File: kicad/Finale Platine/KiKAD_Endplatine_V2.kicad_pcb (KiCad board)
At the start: 2 copper layers, 102 x 50 mm, 57 parts, among them J1 Conn_02x08_Odd_Even, J4 Conn_01x03_Pin, Q1 Q_NPN_ECB, Q2 Q_NPN_ECB, Q3 Q_NPN_ECB, Q4 Q_NPN_ECB, U1 NE555P, U2 TL074

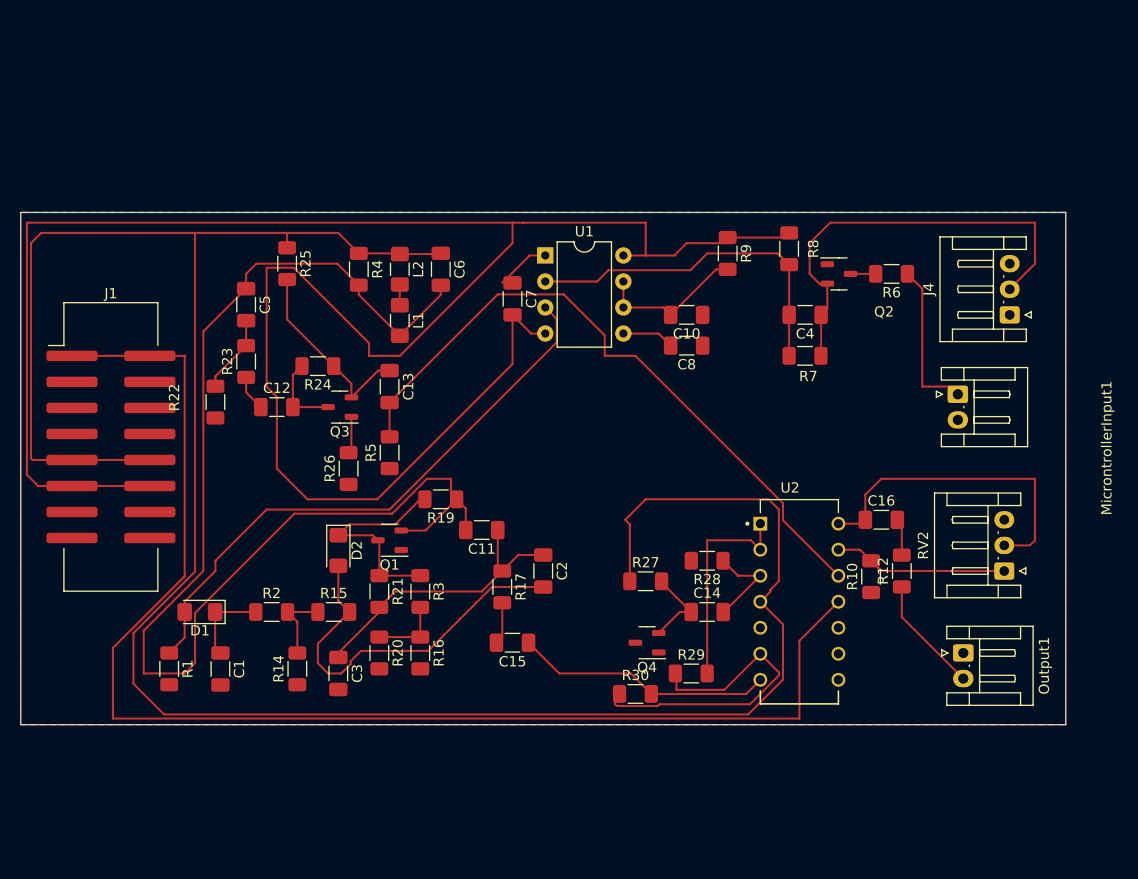
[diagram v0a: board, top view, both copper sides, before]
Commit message: Platinendesign update mit 2 Induktoren
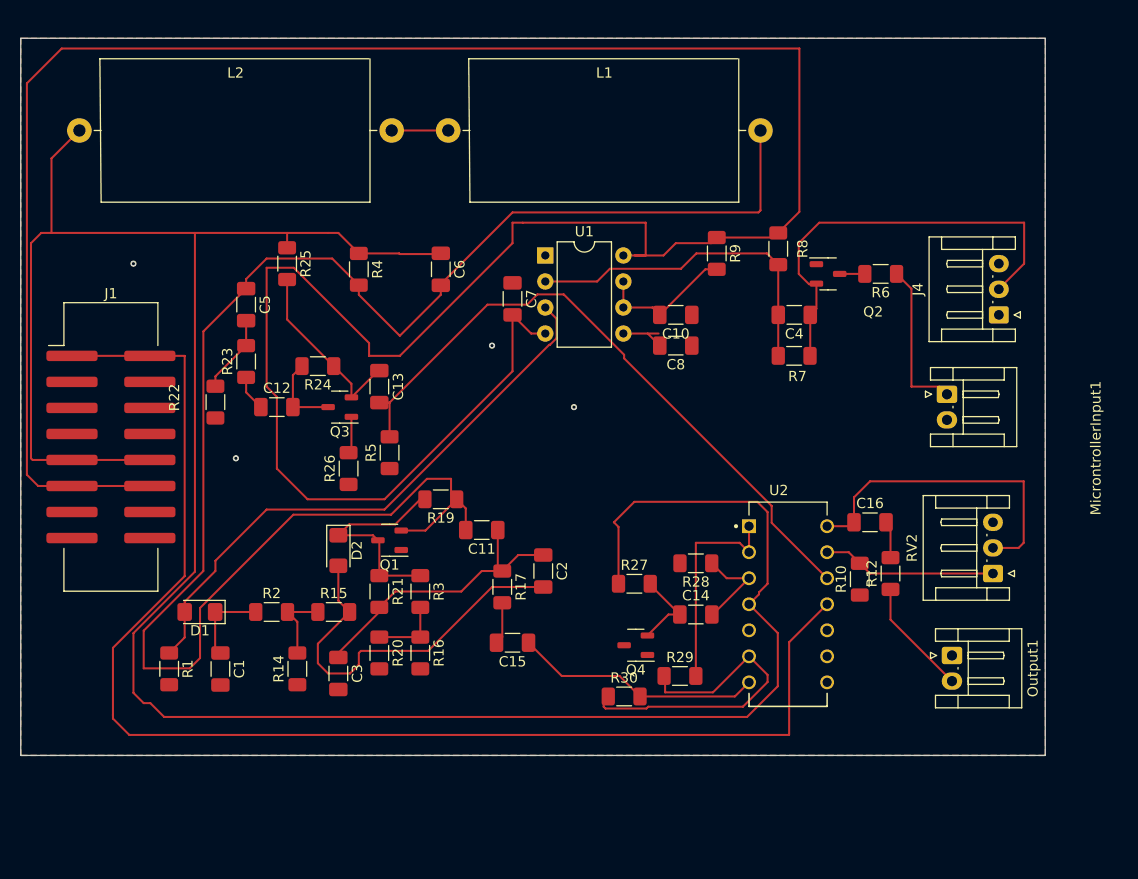
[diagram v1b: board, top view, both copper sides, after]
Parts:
- L1, L2: footprint Inductor_SMD:L_1206_3216Metric_Pad1.42x1.75mm_HandSolder -> TL074:L_Axial_L26.0mm_D14.0mm_P30.48mm_Horizontal_Fastron_JORIS
- moved L2 34.1 mm to (105.7, 44.0), turned to 0 degrees
- moved L1 19.1 mm to (141.7, 44.0), turned to 0 degrees
- moved C14 1.13 mm to (165.9, 91.2)
- moved C16 1.13 mm to (182.9, 82.2)
- moved Output1 1.13 mm to (190.9, 95.2)
- moved Q4 1.13 mm to (160.0, 94.2)
- moved R10 1.13 mm to (181.9, 87.8)
- moved R12 1.13 mm to (184.9, 87.2)
- moved R27 1.13 mm to (159.9, 88.2)
- moved R28 1.13 mm to (165.9, 86.2)
- moved R29 1.13 mm to (164.3, 97.2)
- moved R30 1.13 mm to (158.9, 99.2)
- moved RV2 1.13 mm to (194.9, 87.2)
- moved U2 1.13 mm to (174.9, 90.2)
- moved C10 1.06 mm to (163.9, 62.0)
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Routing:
- net +5V: track 211.4 -> 273.6 mm
- net Net-(Q1-C): track 121.6 -> 163.1 mm
- net +12V: track 228.6 -> 240.4 mm
- net GND: track 5.31 -> 0.00 mm, vias 0 -> 4
- net Net-(L1-Pad1): track 2.02 -> 5.52 mm
- net -12V: track 129.3 -> 130.4 mm
- net Net-(Q3-C): track 18.9 -> 17.8 mm
- net Net-(U1-TR): track 34.3 -> 33.2 mm
- net Net-(C15-Pad1): track 25.3 -> 24.3 mm
- net Net-(C13-Pad2): track 65.0 -> 64.1 mm
- net Net-(D2-A): track 37.3 -> 37.8 mm
- added copper zone on B.Cu, net GND
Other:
- board size 102 x 50 mm -> 100 x 70 mm

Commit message: Platinenupdate
Platine geupdatet Beschriftung mehr oder weniger gut
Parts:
- added +/L3: 100m, Inductor_THT:L_Radial_D12.0mm_P6.00mm_Murata_1900R, F.Cu at (113.0, 43.0)
- added C6/R1: 1000k, Resistor_SMD:R_1206_3216Metric_Pad1.30x1.75mm_HandSolder, F.Cu at (147.0, 110.0)
- added R12/-1: 100, Resistor_SMD:R_1206_3216Metric_Pad1.30x1.75mm_HandSolder, F.Cu at (142.0, 91.0)
- added RV1/-1: 10k, Connector_JST:JST_EH_S3B-EH_1x03_P2.50mm_Horizontal, F.Cu at (147.5, 87.5)
- +/L1: renamed from L1; value 560m -> 100m; footprint TL074:L_Axial_L26.0mm_D14.0mm_P30.48mm_Horizontal_Fastron_JORIS -> Inductor_THT:L_Radial_D12.0mm_P6.00mm_Murata_1900R
- +/L2: renamed from L2; value 560m -> 100m; footprint TL074:L_Axial_L26.0mm_D14.0mm_P30.48mm_Horizontal_Fastron_JORIS -> Inductor_THT:L_Radial_D12.0mm_P6.00mm_Murata_1900R
- D2: value D -> C5/D2
- moved +/L2 20.3 mm to (126.0, 43.0)
- moved C7/+1 13.4 mm to (157.0, 77.0)
- moved R1/R1 13.0 mm to (108.0, 107.8)
- moved R5/D1 12.5 mm to (110.0, 101.0)
- moved D1/R2 11.9 mm to (118.0, 101.0)
- moved +/C15 11.4 mm to (151.0, 105.0)
- moved -/-1 11.4 mm to (142.0, 106.0)
- moved C3/C1 11.3 mm to (119.3, 107.8)
- moved C6/R3 11.2 mm to (137.0, 106.0)
- moved C4/C2 10.4 mm to (147.0, 96.6)
- moved +/R17 10.0 mm to (153.0, 96.5)
- moved R7/-1 10.0 mm to (130.6, 101.0)
- moved R10/-1 9.49 mm to (142.0, 98.0)
- moved R9/+1 9.22 mm to (130.5, 106.2)
- moved +/+1 9.06 mm to (136.0, 98.0)
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- renumbered R21 to +/+1, C14 to +/C14, C15 to +/C15, C6 to +/C6, Q4 to +/Q4, R17 to +/R17, R27 to +/R27, R28 to +/R28, R29 to +/R29, R30 to +/R30, R16 to -/-1, C12 to C1/+1, C1 to C3/C1, C2 to C4/C2, R20 to C6/R3, C11 to C7/+1, C5 to C8/C5, C13 to C9/+1, R2 to D1/R2, Q3 to Q3/+1, R1 to R1/R1, R3 to R10/-1, R19 to R11/+1, R4 to R14/R4, R23 to R16/+1, R26 to R17/+1, R22 to R2/R5, R25 to R3/+1, R24 to R4/+1, D1 to R5/D1, R5 to R6/+1, R15 to R7/-1, R14 to R8/1, C3 to R9/+1
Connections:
- +/L2 pad 1: +12V -> Net-(+/L2-Pad1)
- -/-1 pad 2: GND -> Net-(-/-1-Pad2)
- Q1 pad 1: GND -> Net-(Q1-E)
- R9/+1 pad 2: GND -> Net-(-/-1-Pad2)
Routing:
- net +5V: track 273.6 -> 198.8 mm
- net +12V: track 240.4 -> 283.7 mm
- net -12V: track 130.4 -> 170.9 mm
- net Net-(Q1-C): track 163.1 -> 185.4 mm
- net Net-(+/+1-Pad2): track 28.8 -> 48.7 mm
- net Net-(R5/D1-A): track 56.6 -> 74.9 mm
- net Net-(-/-1-Pad2): track 0.00 -> 17.9 mm
- net Net-(+/R29-Pad1): track 32.9 -> 17.3 mm
- net Net-(C8/C5-Pad2): track 7.64 -> 18.5 mm
- net Net-(R12/-1-Pad1): track 0.00 -> 7.89 mm
- net Net-(Q3/+1-C): track 17.8 -> 25.3 mm
- net Net-(+/L2-Pad1): track 0.00 -> 7.00 mm
- net Net-(Q3/+1-B): track 7.81 -> 13.4 mm
- net Net-(R5/D1-K): track 8.17 -> 13.3 mm
- net Net-(C1/+1-Pad1): track 3.50 -> 8.23 mm
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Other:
- board size 100 x 70 mm -> 100 x 80 mm

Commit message: Schaltplan verschönert
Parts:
- U2: footprint TL074:DIP762W51P254L1994H508Q14 -> Package_DIP:DIP-14_W7.62mm
- moved U2 8.58 mm to (171.2, 82.5)
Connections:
- U2 pad 11: -12V -> (no net)
- U2 pad 4: +12V -> (no net)

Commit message: Namenochmal geupdated
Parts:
- renumbered C10 to C21, C4 to C22, C8 to C23, C7 to C24, R6 to R31, R7 to R32, R8 to R33, R9 to R34
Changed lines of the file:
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@@
     (property "ki_keywords" "capacitor cap")
     (attr smd)
-    (fp_text reference "C4" (at 0 -1.85) (layer "F.SilkS")
+    (fp_text reference "C22" (at 0 -1.85) (layer "F.SilkS")
         (effects (font (size 1 1) (thickness 0.15)))
     )
@@
     (property "ki_keywords" "capacitor cap")
     (attr smd)
-    (fp_text reference "C10" (at 0 -1.85) (layer "F.SilkS")
+    (fp_text reference "C21" (at 0 -1.85) (layer "F.SilkS")
         (effects (font (size 1 1) (thickness 0.15)))
     )
@@
     (property "ki_keywords" "R res resistor")
     (attr smd)
-    (fp_text reference "R8" (at 0 -2.38 90) (layer "F.SilkS")
+    (fp_text reference "R33" (at 0 -2.38 90) (layer "F.SilkS")
         (effects (font (size 1 1) (thickness 0.15)))
     )
@@
     (property "ki_keywords" "capacitor cap")
     (attr smd)
-    (fp_text reference "C8" (at 0 -1.85) (layer "F.SilkS")
+    (fp_text reference "C23" (at 0 -1.85) (layer "F.SilkS")
         (effects (font (size 1 1) (thickness 0.15)))
     )
@@
     (property "ki_keywords" "R res resistor")
     (attr smd)
-    (fp_text reference "R7" (at 0.325 2) (layer "F.SilkS")
+    (fp_text reference "R32" (at 0.325 2) (layer "F.SilkS")
         (effects (font (size 1 1) (thickness 0.15)))
     )
@@
     (property "ki_keywords" "R res resistor")
     (attr smd)
-    (fp_text reference "R9" (at 0 -1.82 90) (layer "F.SilkS")
+    (fp_text reference "R34" (at 0 -1.82 90) (layer "F.SilkS")
         (effects (font (size 1 1) (thickness 0.15)))
     )
@@
     (property "ki_keywords" "R res resistor")
     (attr smd)
-    (fp_text reference "R6" (at 0 -1.82) (layer "F.SilkS")
+    (fp_text reference "R31" (at 0 -1.82) (layer "F.SilkS")
         (effects (font (size 1 1) (thickness 0.15)))
     )
@@
     (property "ki_keywords" "capacitor cap")
     (attr smd)
-    (fp_text reference "C7" (at 0 -1.85 90) (layer "F.SilkS")
-        (effects (font (size 1 1) (thickness 0.15)))
-    )
+    (fp_text reference "C24" (at 0 -1.85 90) (layer "F.SilkS")
+        (effects (font (size 1 1) (thickness 0.15)))
+    )

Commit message: kicad überarbeitung
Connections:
- RV2 pad 3: unconnected-(RV2-Pad3) -> Net-(C16-Pad1)
- U2 pad 11: (no net) -> -12V
- U2 pad 4: (no net) -> +12V
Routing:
- net Net-(D2-A): track 42.1 -> 41.4 mm

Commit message: PLATINE endlich fertig glaube ich
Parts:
- added +/R1: 100k, Resistor_SMD:R_1206_3216Metric_Pad1.30x1.75mm_HandSolder, F.Cu at (184.5, 79.0)
- added +/RV1: 10k, Connector_JST:JST_EH_S3B-EH_1x03_P2.50mm_Horizontal, F.Cu at (187.5, 100.5)
- added +/RV2: 10k, Connector_JST:JST_EH_S3B-EH_1x03_P2.50mm_Horizontal, F.Cu at (135.0, 112.0)
- added +/RV3: 10k, Connector_JST:JST_EH_S3B-EH_1x03_P2.50mm_Horizontal, F.Cu at (183.5, 87.5)
- added C1: C, Capacitor_SMD:C_1206_3216Metric_Pad1.33x1.80mm_HandSolder, F.Cu at (189.0, 88.0)
- added REF**: MountingHole_3.2mm_M3, MountingHole:MountingHole_3.2mm_M3, F.Cu at (103.5, 111.5)
- added REF**: MountingHole_3.2mm_M3, MountingHole:MountingHole_3.2mm_M3, F.Cu at (103.5, 38.5)
- added RV/+1: 10k, Connector_JST:JST_EH_S3B-EH_1x03_P2.50mm_Horizontal, F.Cu at (112.5, 92.5)
- added RV/RV/+1: 10k, Connector_JST:JST_EH_S3B-EH_1x03_P2.50mm_Horizontal, F.Cu at (119.0, 101.0)
- D2: value C5/D2 -> C5/D2/D2
- MicrontrollerInput1, Output1: footprint Connector_JST:JST_EH_S2B-EH_1x02_P2.50mm_Horizontal -> Connector_JST:JST_EH_S3B-EH_1x03_P2.50mm_Horizontal
- moved Output1 38.7 mm to (191.0, 56.5)
- moved MicrontrollerInput1 25.3 mm to (190.5, 44.5)
- moved R31 23.8 mm to (196.0, 37.5)
- moved C22 21.7 mm to (184.0, 43.5)
- moved Q2 21.3 mm to (187.4, 38.5)
- moved R32 21.2 mm to (184.0, 49.0)
- moved R12 19.9 mm to (187.5, 67.5)
- moved C21 18.0 mm to (173.0, 46.5)
- moved U2 17.7 mm to (170.2, 64.9)
- moved C23 17.5 mm to (173.0, 50.0)
- moved C24 17.1 mm to (155.5, 45.6)
- moved R34 17.1 mm to (172.5, 39.5)
- moved +/C15 17.0 mm to (168.0, 105.0)
- moved C6/R1/C3 17.0 mm to (164.0, 110.0)
- moved U1 16.7 mm to (160.0, 42.0)
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- renumbered +/C6 to +/C6/C6, R5/D1 to +/D1, +/L2 to +/L2/L2, -/-1 to -/-/-1, C1/+1 to C1/+/-1, C4/C2 to C4/C2/C2, C6/R1 to C6/R1/C3, C7/+1 to C7/+/+1, C8/C5 to C8/C5/C5, C9/+1 to C9/+/-1, D1/R2 to D1/R2/R2, Q3/+1 to Q3/+1/+1, R1/R1 to R1/R1/R1, R11/+1 to R11/+/+1, R14/R4 to R14/R4/R4, R16/+1 to R16/+1/R5, R17/+1 to R17/+/+1, R2/R5 to R2/R5/+1, R3/+1 to R3/+/+1, R4/+1 to R4/+/-1, R6/+1 to R6/+/+1, R7/-1 to R7/-/-1, R8/1 to R8/1/+1, R9/+1 to R9/+/+1, RV1/-1 to RV1k/-/-1
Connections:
- +/R29 pad 1: Net-(U2B--) -> Net-(+/R29-Pad1)
- +/R29 pad 2: Net-(U2A--) -> Net-(U2B--)
- +/R30 pad 1: Net-(U2B--) -> Net-(+/R30-Pad1)
- D1/R2/R2 pad 2: Net-(D1/R2-Pad2) -> Net-(D1/R2/R2-Pad2)
- R7/-/-1 pad 1: Net-(D1/R2-Pad2) -> Net-(D1/R2/R2-Pad2)
- R8/1/+1 pad 2: Net-(D1/R2-Pad2) -> Net-(R8/1/+1-Pad2)
- RV1k/-/-1 pad 1: unconnected-(RV1/-1-Pad1) -> Net-(R12/-1-Pad1)
- RV1k/-/-1 pad 2: Net-(R12/-1-Pad1) -> GND
- RV2 pad 3: Net-(C16-Pad1) -> unconnected-(RV2-Pad3)
- U2 pad 10: unconnected-(U2C-+-Pad10) -> Net-(U2A--)
- U2 pad 8: unconnected-(U2-Pad8) -> Net-(+/R29-Pad1)
- U2 pad 9: unconnected-(U2C---Pad9) -> Net-(U2C--)
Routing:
- net Net-(Q1-C): track 185.4 -> 79.9 mm
- net Net-(U2D-+): track 59.5 -> 141.4 mm
- net Net-(+/+1-Pad2): track 48.7 -> 121.6 mm
- net Net-(+/R29-Pad1): track 0.00 -> 52.2 mm
- net -12V: track 171.0 -> 220.5 mm
- net +5V: track 198.8 -> 149.8 mm
- net Net-(J4-Pin_2): track 46.8 -> 17.0 mm
- net Net-(+/RV2-Pad2): track 9.90 -> 39.2 mm
- net Net-(U2B--): track 17.3 -> 40.4 mm
- net +12V: track 283.8 -> 264.0 mm
- net Net-(+/C15-Pad1): track 22.7 -> 42.2 mm
- net Net-(U2C--): track 0.00 -> 18.4 mm
- net Net-(D2-A): track 41.4 -> 25.2 mm
- net Net-(D1/R2/R2-Pad2): track 0.00 -> 16.0 mm
- net Net-(U2A-+): track 9.34 -> 23.2 mm
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
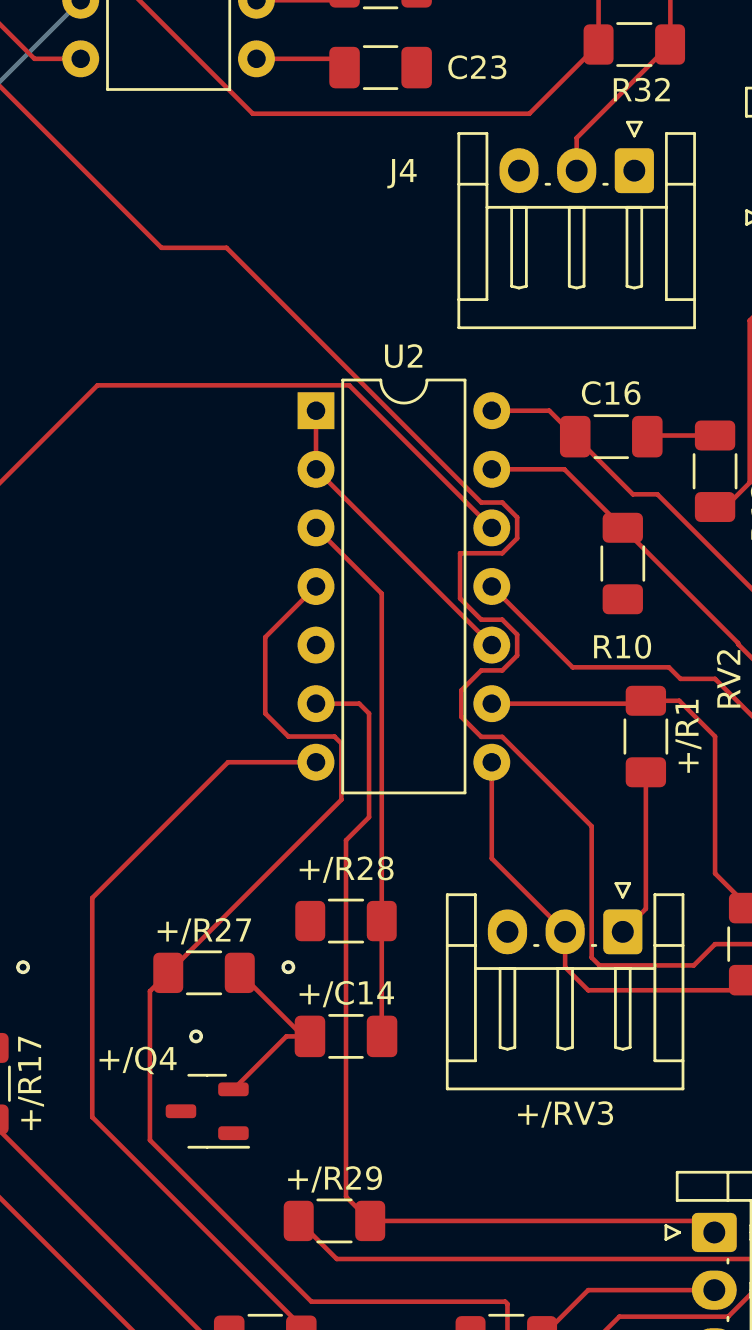
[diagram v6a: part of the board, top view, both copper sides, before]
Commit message: Beschriftung verändert
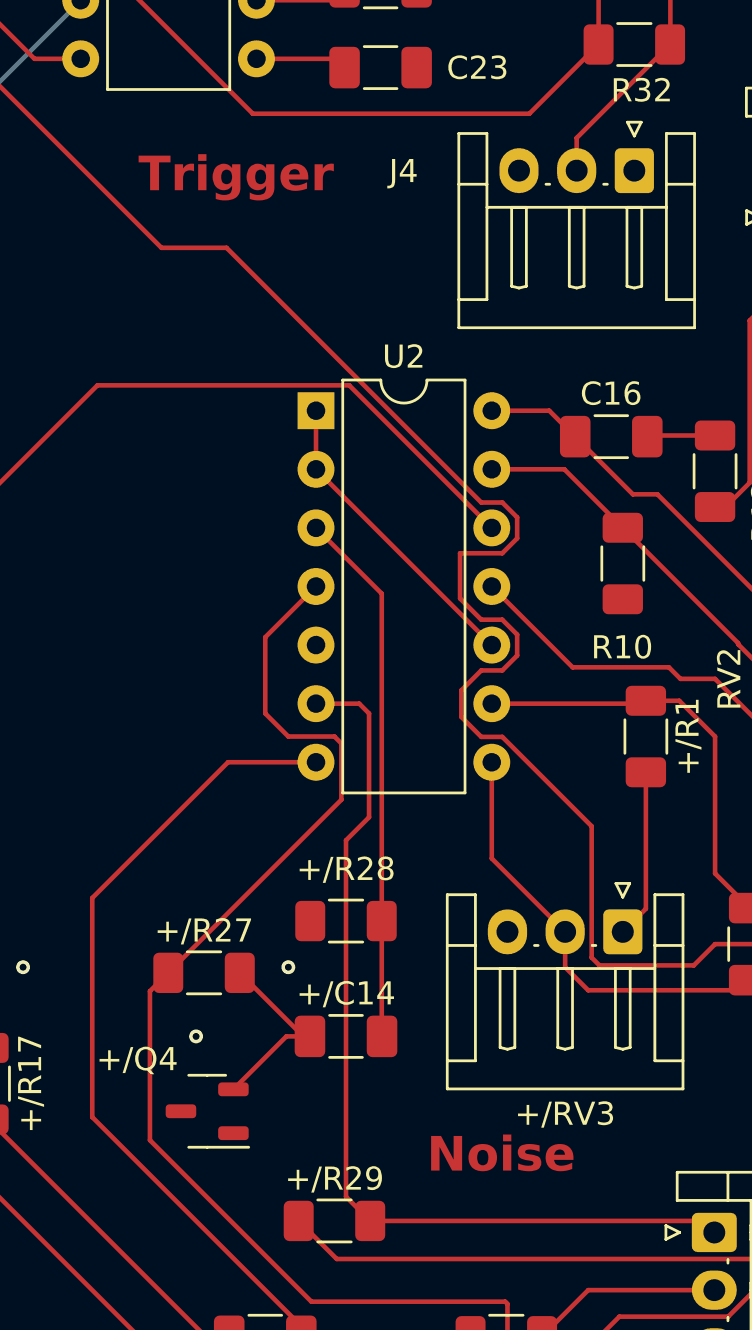
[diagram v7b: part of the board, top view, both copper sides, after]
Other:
- board text added: "Noise"
- board text added: "Trigger"
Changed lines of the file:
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@@
   (gr_rect (start 100 35) (end 200 115)
     (stroke (width 0.05) (type default)) (fill none) (layer "Edge.Cuts"))
+  (gr_text "Trigger" (at 162.5 55.5) (layer "F.Cu")
+    (effects (font (size 1.5 1.5) (thickness 0.3) bold) (justify left bottom))
+  )
+  (gr_text "Noise\n" (at 175 98) (layer "F.Cu")
+    (effects (font (size 1.5 1.5) (thickness 0.3) bold) (justify left bottom))
+  )
   (segment (start 154 72) (end 151.0625 69.0625) (width 0.2) (layer "F.Cu") (net 1))
   (segment (start 136 99.55) (end 141.1125 99.55) (width 0.2) (layer "F.Cu") (net 1))
